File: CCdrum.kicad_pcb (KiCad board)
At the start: 2 copper layers, 75 x 40 mm, 28 parts, among them J1 USB_B_μ, J3 MIDI_out, J4 Program, U1 MSP430G2533, U2 AMS1117-3.3, U3 74AUP1G17

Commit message: Re-annotated components
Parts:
- C1: value 330n -> 330
- C2: value 100n -> 100
- renumbered D7 to D6, J4 to J2, R7 to R2, R8 to R3, R11 to R4, R12 to R5, R13 to R6, R15 to R7, R10 to R8
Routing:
- net +3V3: track 3.23 -> 6.42 mm

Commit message: New PCB Arrangement
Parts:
- added RV6: 10k, w_pth_resistors:trimmer_alps-rk09k1130ah1, F.Cu at (37.3, 154.2)
- added SW1: SW_Push, Button_Switch_THT:SW_PUSH_6mm_H4.3mm, F.Cu at (119.2, 151.0)
- added SW2: SW_Push, Button_Switch_THT:SW_PUSH_6mm_H4.3mm, F.Cu at (122.6, 157.5)
- D1: value BIT -> 1
- D2: value FLD -> 2
- D3: value DRV -> 3
- D4: value PAN -> 4
- D5: value GAN -> 5
- D6: value ON -> 6
- moved R4 104.1 mm to (56.9, 137.2), turned to 90 degrees
- moved R2 101.6 mm to (49.8, 137.2), turned to 90 degrees
- moved R3 101.0 mm to (53.3, 137.2), turned to 90 degrees
- moved J2 95.9 mm to (32.0, 126.8)
- moved C1 95.4 mm to (37.2, 137.5), turned to 90 degrees
- moved D5 93.9 mm to (92.7, 142.2)
- moved D4 92.8 mm to (78.8, 142.2)
- moved D3 91.6 mm to (65.0, 142.2)
- moved D2 90.5 mm to (51.1, 142.2)
- moved D1 89.4 mm to (37.3, 142.2)
- moved J1 89.1 mm to (32.8, 134.8)
- moved U2 87.7 mm to (43.4, 134.9)
- moved R5 86.5 mm to (90.5, 137.2), turned to 90 degrees
- moved R6 86.3 mm to (94.0, 137.2), turned to 90 degrees
- moved C2 83.6 mm to (47.7, 127.8), turned to 180 degrees
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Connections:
- net LED_DRV renamed LED_P3
- net LED_GAN renamed LED_P5
- R2 pad 1: LED_BIT -> LED_P1
- R3 pad 1: LED_FLD -> LED_P2
- R5 pad 1: LED_PAN -> LED_P4
- R7 pad 1: LED_STATUS -> LED_P6
- R8 pad 1: Net-(J3-Pad4) -> Net-(J3-Pad5)
- R8 pad 2: GND -> Net-(R8-Pad2)
- R9 pad 1: Net-(J3-Pad5) -> Net-(J3-Pad4)
- R9 pad 2: Net-(R9-Pad2) -> GND
- U1 pad 10: LED_FLD -> LED_P4
- U1 pad 12: LED_PAN -> LED_P2
- U1 pad 13: LED_STATUS -> LED_P1
- U1 pad 14: Net-(U1-Pad14) -> GAN
- U1 pad 15: GAN -> PART
- U1 pad 8: LED_BIT -> LED_P6
- U3 pad 4: Net-(R9-Pad2) -> Net-(R8-Pad2)
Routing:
- net GAN: track 39.7 -> 0.00 mm
- net Net-(D3-Pad2): track 38.4 -> 0.00 mm
- net RST: track 34.6 -> 0.00 mm, vias 2 -> 0
- net LED_FLD: track 32.6 -> 0.00 mm
- net TEST: track 30.1 -> 0.00 mm
- net Net-(D6-Pad2): track 29.7 -> 0.00 mm, vias 1 -> 0
- net TXD: track 29.2 -> 0.00 mm
- net BIT: track 23.0 -> 0.00 mm
- net Net-(D1-Pad2): track 23.0 -> 0.00 mm
- net Net-(D2-Pad2): track 22.9 -> 0.00 mm
- net Net-(D5-Pad2): track 22.1 -> 0.00 mm
- net LED_BIT: track 20.2 -> 0.00 mm, vias 1 -> 0
- net Net-(J3-Pad5): track 19.7 -> 0.00 mm
- net PAN: track 19.4 -> 0.00 mm
- net FLD: track 16.0 -> 0.00 mm
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- removed copper zone on B.Cu, net +3V3
- removed copper zone on F.Cu, net GND
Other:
- board size 75 x 40 mm -> 100 x 35 mm
- board text added: "1"
- board text added: "2"
- board text added: "3"
- board text added: "4"
- board text added: "5"
- board text added: "6"
- board text added: "BIT"
- board text added: "CCVDrum for Korg Volca Drum github.com/sensai7/CCVDrum"
- board text added: "DRV"
- board text added: "FLD"
- board text added: "G"
- board text added: "GAN"
- board text added: "PAN"
- board text added: "PART"
- board text added: "R"
- board text added: "T"
- board text added: "V"
- board text removed: "3.3V"
- board text removed: "CCVDrum V0.1"
- board text removed: "GND"
- board text removed: "RST"
- board text removed: "TEST"

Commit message: PCB Routed
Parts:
- moved SW2 7.93 mm to (127.2, 151.0), turned to 270 degrees
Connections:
- U1 pad 18: Net-(U1-Pad18) -> PUSH_L1
- U1 pad 19: Net-(U1-Pad19) -> PUSH_L2
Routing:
- net PUSH_L2: track 0.00 -> 82.6 mm
- net PUSH_L1: track 0.00 -> 72.3 mm
- net LED_P6: track 0.00 -> 54.3 mm
- net PART: track 0.00 -> 47.5 mm
- net TEST: track 0.00 -> 41.4 mm
- net RST: track 0.00 -> 41.3 mm
- net TXD: track 0.00 -> 40.8 mm, vias 0 -> 2
- net +3V3: track 0.00 -> 38.6 mm
- net LED_P5: track 0.00 -> 37.9 mm, vias 0 -> 1
- net GAN: track 0.00 -> 35.3 mm
- net LED_P1: track 0.00 -> 35.2 mm, vias 0 -> 1
- net LED_P2: track 0.00 -> 34.2 mm, vias 0 -> 1
- net LED_P3: track 0.00 -> 33.2 mm, vias 0 -> 1
- net Net-(D4-Pad2): track 0.00 -> 20.0 mm
- net Net-(D1-Pad2): track 0.00 -> 20.0 mm
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- added copper zone on B.Cu, net +3V3
- added copper zone on F.Cu, net GND

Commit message: New PCB design
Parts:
- added C3: 1n, Capacitor_THT:C_Disc_D5.0mm_W2.5mm_P5.00mm, F.Cu at (56.7, 125.1)
- added C4: 10, Capacitor_THT:C_Disc_D5.0mm_W2.5mm_P5.00mm, F.Cu at (65.6, 125.1)
- added C5: 100, Capacitor_THT:C_Disc_D5.0mm_W2.5mm_P5.00mm, F.Cu at (69.6, 125.1)
- added R10: 1k, Resistor_THT:R_Axial_DIN0207_L6.3mm_D2.5mm_P7.62mm_Horizontal, F.Cu at (60.4, 135.7)
- moved R4 11.5 mm to (63.9, 128.1), turned to 270 degrees
- moved R7 11.5 mm to (104.6, 128.1), turned to 270 degrees
- moved U3 9.99 mm to (115.4, 143.1), turned to 180 degrees
- moved R5 9.76 mm to (94.0, 128.1), turned to 270 degrees
- moved R6 9.76 mm to (97.5, 128.1), turned to 270 degrees
- moved R3 9.12 mm to (53.3, 128.1), turned to 270 degrees
- moved R2 9.12 mm to (49.8, 128.1), turned to 270 degrees
- moved J3 4.10 mm to (120.3, 131.7)
- moved R1 3.87 mm to (56.9, 135.7)
- moved U1 3.80 mm to (67.5, 135.7)
- moved R9 3.76 mm to (108.1, 135.7)
- moved C1 2.90 mm to (37.1, 134.6)
- moved U2 2.90 mm to (43.3, 132.0)
- moved J1 2.90 mm to (32.7, 131.9)
- moved C2 2.70 mm to (47.7, 125.1)
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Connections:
- R1 pad 2: RST -> Net-(C3-Pad1)
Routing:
- net +3V3: track 38.6 -> 165.4 mm, vias 0 -> 1
- net LED_P6: track 54.3 -> 23.1 mm, vias 0 -> 1
- net RST: track 41.3 -> 66.7 mm
- net LED_P5: track 37.9 -> 14.2 mm
- net PUSH_L2: track 82.6 -> 105.5 mm, vias 0 -> 3
- net Net-(R8-Pad2): track 10.6 -> 31.3 mm
- net PUSH_L1: track 72.3 -> 89.6 mm, vias 0 -> 3
- net TXD: track 40.8 -> 56.9 mm
- net Net-(D3-Pad2): track 18.7 -> 6.26 mm
- net Net-(D6-Pad2): track 19.0 -> 7.23 mm
- net Net-(C3-Pad1): track 0.00 -> 8.04 mm
- net Net-(D2-Pad2): track 13.1 -> 5.88 mm
- net Net-(D5-Pad2): track 13.8 -> 7.37 mm
- net BIT: track 19.7 -> 24.4 mm
- net FLD: track 13.9 -> 18.2 mm
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- added copper zone on B.Cu, net GND
- removed copper zone on B.Cu, net +3V3
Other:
- board size 100 x 35 mm -> 100 x 37.4 mm
- board text added: "CCVDrum V0.2 for Korg Volca Drum"
- board text added: "github.com/sensai7/CCVDrum"
- board text removed: "CCVDrum for Korg Volca Drum github.com/sensai7/CCVDrum"

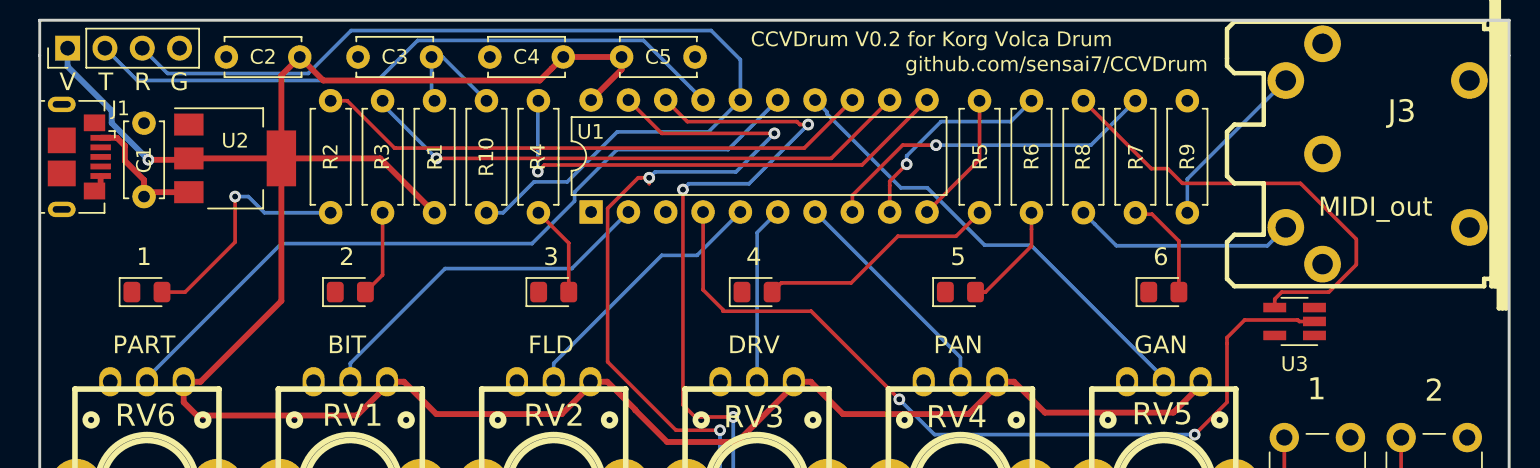
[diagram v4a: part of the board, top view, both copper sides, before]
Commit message: USB changed, small errors on board
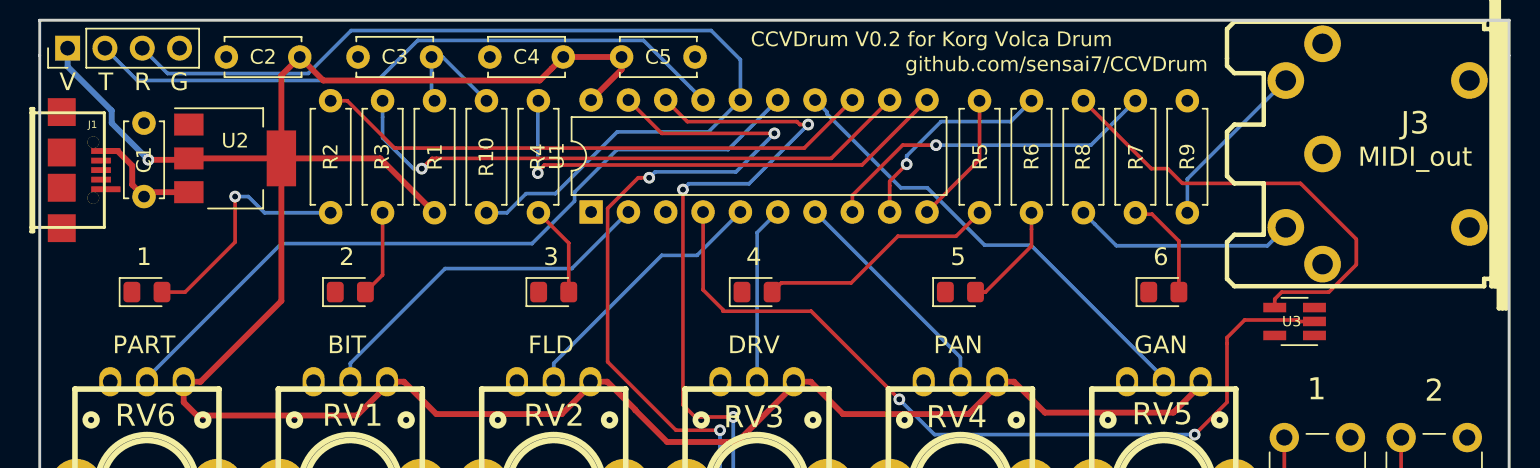
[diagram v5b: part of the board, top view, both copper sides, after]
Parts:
- J1: footprint Connector_USB:USB_Micro-B_GCT_USB3076-30-A -> w_conn_pc:conn_usb_B_micro_smd-2
- moved J1 1.50 mm to (31.5, 132.8)
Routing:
- net LED_P2: track 37.9 -> 40.1 mm
- net +5V: track 9.04 -> 7.82 mm
- net GND: track 1.19 -> 0.00 mm
- net PUSH_L2: track 105.5 -> 104.7 mm
